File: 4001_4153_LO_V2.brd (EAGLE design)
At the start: 109 x 63 mm, 112 parts, among them IC1 74LVC2G17GV,125, IC10 MCP6H01, IC2 74LVC2G17GV,125, IC3 74LVC2G17GV,125, IC4 ADF4001BRUZ, IC5 ATTINY45V-10SU, IC6 7805DT, IC7 7809DT, IC8 LD1117AS33TR, IC9 ADF4153BRUZ-RL7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

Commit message: JLC release
As issued to JLC
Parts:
- added C4: 100nF, rcl:C0603
- added IC11: TL431AIDBZR, RF:SOT23L
- added R30: 470R, rcl:R0603
- added R31, R32: 10K, rcl:R0603
- IC10: value MCP6H01 -> MCP6H01T-E/LT
- moved C23 27.7 mm to (36.9, 5.57), turned to 270 degrees
- moved C20 12.6 mm to (13.9, 34.4), turned to 90 degrees
- moved C21 12.0 mm to (11.9, 34.4), turned to 90 degrees
- moved LSP1 11.0 mm to (17.9, 23.2)
- moved IC7 4.91 mm to (9.24, 29.0), turned to 90 degrees
- moved TXFMR1 4.02 mm to (11.2, 44.9)
- moved C19 2.84 mm to (11.5, 23.3), turned to 180 degrees
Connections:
- new net +5V_PRECISION: C4.1, IC11.G, R30.2, R32.2, VR1.3
- new net N$42: IC11.S, R31.2, R32.1
- net +12V: now also R30.1
- net +5V: no longer VR1.3
- net GND: now also C4.2, IC11.D, R31.1, TXFMR1.1, TXFMR1.6; no longer TXFMR1.3, TXFMR1.4
- net N$33: now also TXFMR1.4; no longer TXFMR1.6
- net N$34: now also TXFMR1.3; no longer TXFMR1.1
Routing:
- net +5V_PRECISION: track 0.00 -> 42.2 mm, vias 0 -> 1
- net +5V: track 158.1 -> 128.1 mm
- net +12V: track 52.0 -> 63.6 mm, vias 2 -> 4
- net N$42: track 0.00 -> 4.41 mm
- net GND: track 59.0 -> 54.9 mm, vias 188 -> 193
- net +9V: track 125.0 -> 128.1 mm

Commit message: various
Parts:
- removed R19: 51R, rcl:R0603
- C22: value 100nF -> 100pF; device rcl:C0805 -> resistor:C0603
- IC10: value MCP6H01T-E/LT -> TS971ILT
- R18: value 18K -> 22R
- moved C23 29.3 mm to (66.2, 5.72), turned to 0 degrees
- moved C29 18.5 mm to (65.6, 24.7), turned to 90 degrees
- moved C22 7.57 mm to (81.4, 21.8), turned to 90 degrees
- moved R21 5.57 mm to (85.6, 6.35)
- turned OSC1 to 180 degrees
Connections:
- removed net CLK: IC4.11, IC9.11
- new net +5V_VCO: L6.2
- net +9V: no longer C22.1, L6.2
- net GND: no longer R19.1
- net N$1: now also C22.1; no longer R19.2
- net SCK: now also IC4.11, IC9.11
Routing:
- net SCK: track 5.78 -> 60.8 mm, vias 0 -> 1
- net 20_MHZ: track 63.2 -> 26.8 mm
- net CLK: track 28.6 -> 0.00 mm
- net +9V: track 128.1 -> 109.7 mm, vias 3 -> 2
- net N$32: track 39.8 -> 27.3 mm
- net MOSI: track 9.37 -> 19.1 mm
- net MISO: track 17.4 -> 11.8 mm
- net 10MHZ_REF: track 14.4 -> 19.9 mm
- net GND: track 54.9 -> 51.2 mm, vias 193 -> 201
- net +3V3: track 276.7 -> 274.0 mm
- net N$8: track 6.09 -> 3.69 mm
- net +5V: track 128.1 -> 130.2 mm
- net LOOP_IN: track 11.6 -> 12.8 mm

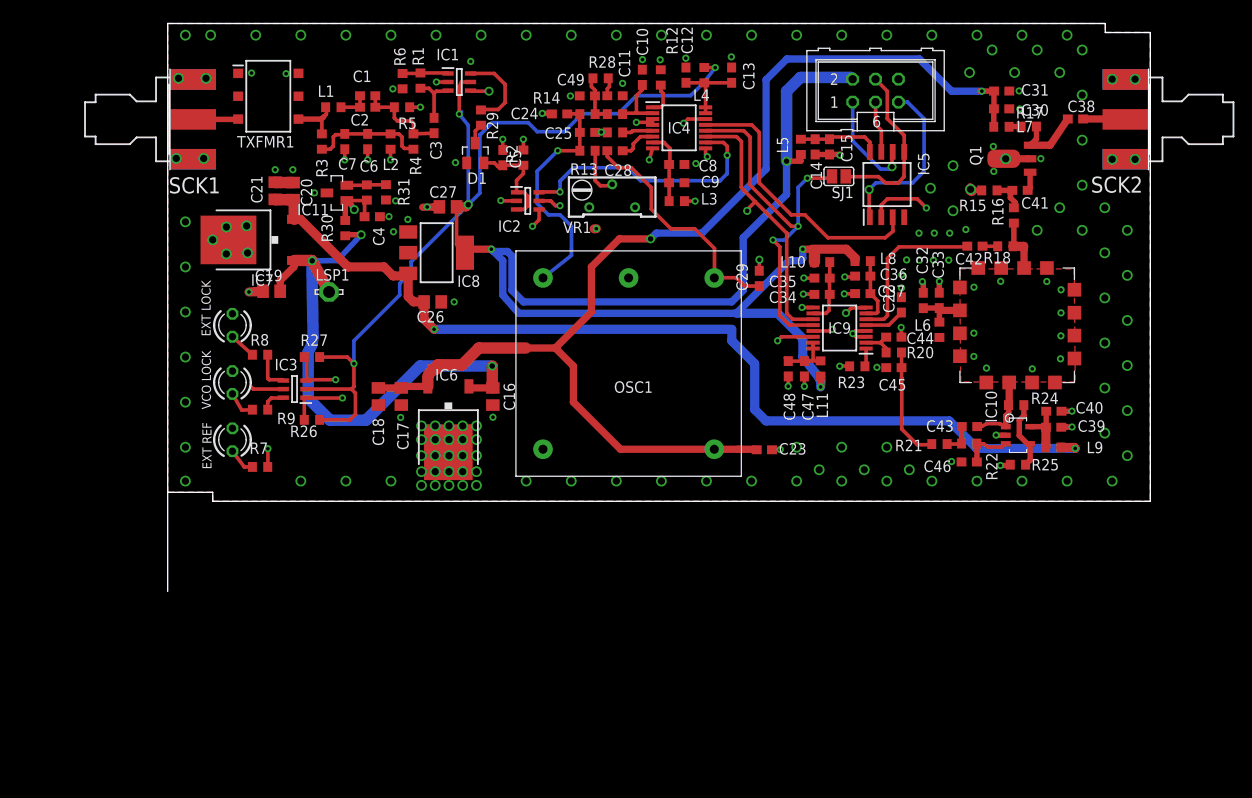
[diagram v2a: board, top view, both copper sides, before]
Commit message: filter loop update
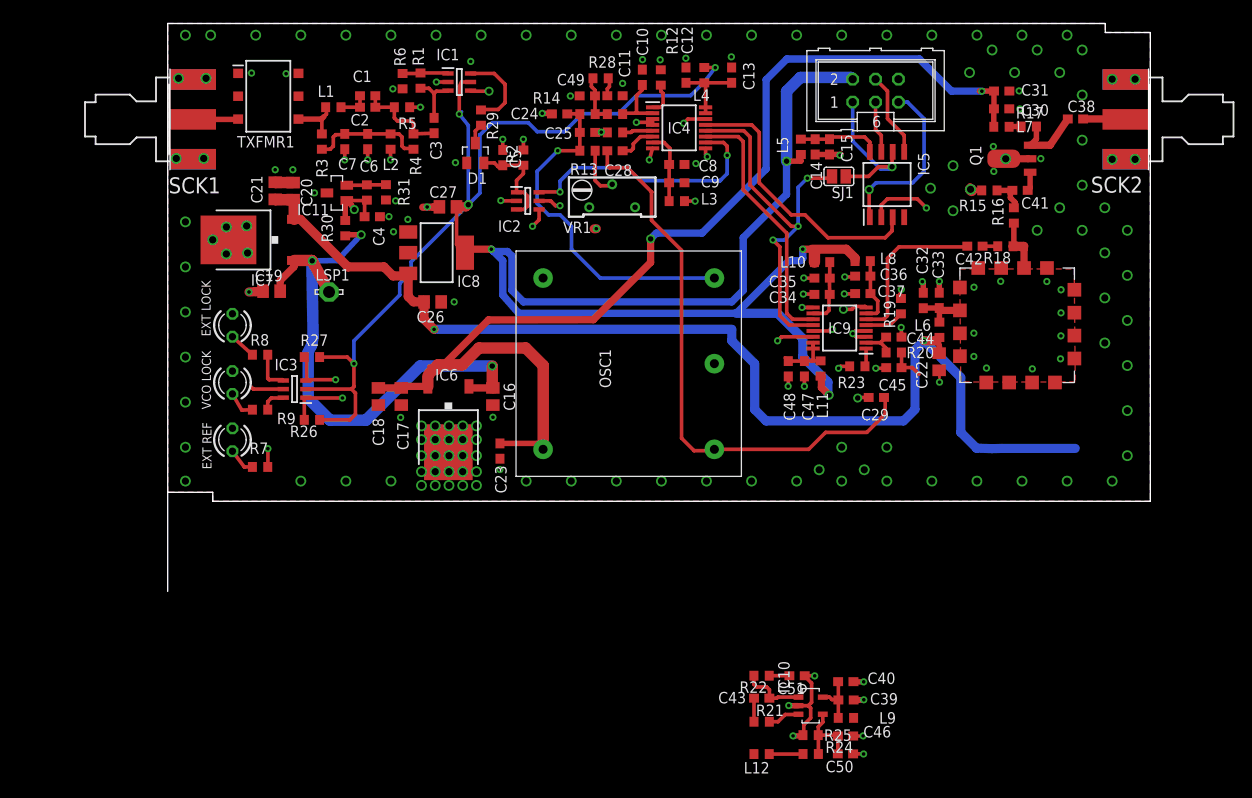
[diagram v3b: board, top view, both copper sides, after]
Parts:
- added C50: 100pF, resistor:C0603
- added C51: 100nF, resistor:C0603
- added L12: 100nH, resistor:R0603
- added R19: 51R, rcl:R0603
- C22: value 100pF -> 100nF; device resistor:C0603 -> rcl:C0805
- C43: value 6.8nF -> 27nF
- C44: value 22nF -> 10nF
- C45: value 10nF -> 1.2nF
- C46: value 15nF -> 100nF
- IC10: value TS971ILT -> MCP6H01T-E/LT
- R18: value 22R -> 18K
- R21: value 27k -> 560R
- R22: value 39k -> 560R
- R24: value 18K -> 10K
- moved R24 44.9 mm to (71.3, -28.0)
- moved C39 38.0 mm to (75.2, -22.0)
- moved C43 37.9 mm to (65.9, -21.8)
- moved C40 37.8 mm to (75.2, -20.0)
- moved IC10 37.8 mm to (71.3, -22.7)
- moved L9 37.8 mm to (75.2, -24.0)
- moved R25 37.8 mm to (71.3, -25.9)
- moved R21 36.6 mm to (65.9, -24.4)
- moved R22 34.5 mm to (65.9, -19.3), turned to 180 degrees
- moved C46 33.4 mm to (75.2, -26.0), turned to 180 degrees
- moved C23 29.3 mm to (36.9, 5.57), turned to 270 degrees
- moved C29 18.5 mm to (78.6, 11.5), turned to 180 degrees
- moved C22 7.57 mm to (85.6, 15.5), turned to 270 degrees
- turned OSC1 to 90 degrees
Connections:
- removed net +5V_VCO: L6.2
- removed net N$6: C43.2, IC10.P$1, OSC2.P$2, R24.2
- new net CLK: IC4.11, IC9.11
- new net N$39: L12.1, R24.2
- new net N$40: C51.2, OSC2.P$2, R22.1
- net +3V3: now also L12.2
- net +9V: now also C22.1, L6.2
- net GND: now also C50.1, C51.1, R19.1
- net LOOP_IN: now also IC10.P$3, R21.2; no longer R21.1
- net N$1: now also R19.2; no longer C22.1
- net N$5: now also C46.2, C50.2
- net N$8: now also R21.1; no longer R21.2, R22.1
- net N$9: now also C43.2, IC10.P$1; no longer C46.2, IC10.P$3
- net SCK: no longer IC4.11, IC9.11
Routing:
- net SCK: track 60.8 -> 5.78 mm, vias 1 -> 0
- net 20_MHZ: track 26.8 -> 63.2 mm
- net CLK: track 0.00 -> 28.6 mm
- net +9V: track 109.7 -> 126.5 mm
- net GND: track 51.2 -> 66.5 mm, vias 201 -> 191
- net N$32: track 27.3 -> 39.8 mm
- net MOSI: track 19.1 -> 9.37 mm
- net N$6: track 8.55 -> 0.00 mm
- net MISO: track 11.8 -> 17.4 mm
- net 10MHZ_REF: track 19.9 -> 14.4 mm
- net LOOP_IN: track 12.8 -> 7.67 mm
- net N$39: track 0.00 -> 3.75 mm
- net +3V3: track 274.0 -> 276.7 mm
- net N$40: track 0.00 -> 2.24 mm
- net +5V: track 130.2 -> 128.1 mm
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
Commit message: Layout
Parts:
- added C52: DNF, resistor:C0603
- moved L12 44.5 mm to (87.1, 11.0), turned to 0 degrees
- moved R24 40.4 mm to (81.7, 11.0), turned to 0 degrees
- moved C50 39.1 mm to (77.8, 11.0), turned to 0 degrees
- moved R21 37.8 mm to (87.1, 6.86), turned to 180 degrees
- moved R25 36.4 mm to (81.7, 8.94), turned to 0 degrees
- moved C46 35.2 mm to (77.8, 9.03), turned to 0 degrees
- moved R22 34.4 mm to (90.4, 4.80)
- moved C43 34.1 mm to (87.1, 4.84), turned to 180 degrees
- moved C51 33.4 mm to (90.4, 6.90), turned to 0 degrees
- moved IC10 30.2 mm to (81.7, 5.67), turned to 180 degrees
- moved L9 29.1 mm to (72.5, 4.99), turned to 180 degrees
- moved C39 27.2 mm to (77.8, 5.03), turned to 180 degrees
- moved C40 27.2 mm to (77.8, 7.04), turned to 180 degrees
- moved C29 9.27 mm to (69.4, 10.5), turned to 0 degrees
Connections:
- net LOOP_IN: now also C52.1
- net N$8: now also C52.2
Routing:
- net +3V3: track 276.7 -> 294.0 mm, vias 10 -> 11
- net 20_MHZ: track 63.2 -> 52.4 mm
- net GND: track 66.5 -> 55.8 mm, vias 191 -> 187
- net LOOP_IN: track 7.67 -> 16.4 mm, vias 0 -> 2
- net N$40: track 2.24 -> 9.68 mm
- net N$3: track 5.95 -> 10.9 mm
- net 10MHZ_REF: track 14.4 -> 16.5 mm
- net +9V: track 126.5 -> 124.3 mm, vias 2 -> 4
- net N$9: track 7.15 -> 8.73 mm
- net N$8: track 2.61 -> 4.04 mm

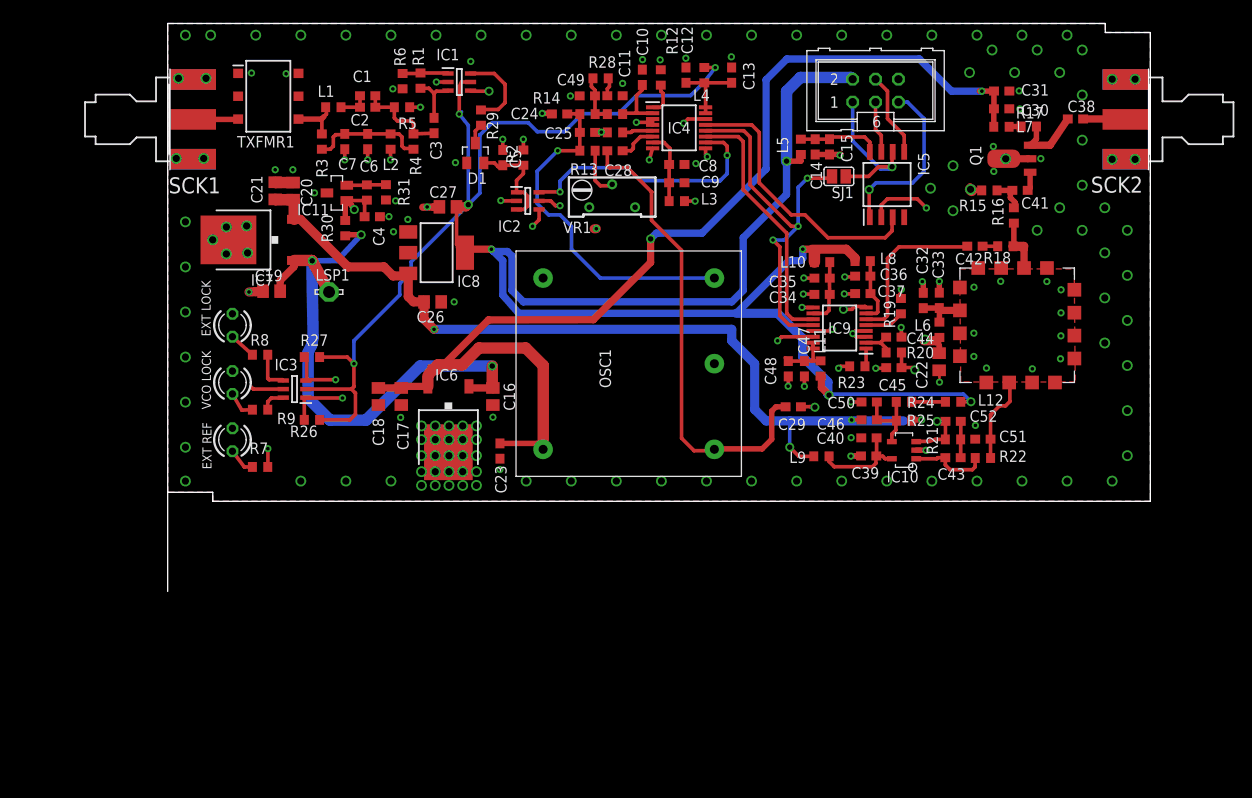
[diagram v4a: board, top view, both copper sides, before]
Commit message: Ref synth updates
Firmware working for ADF4001
Various board updates, ref input still needs works
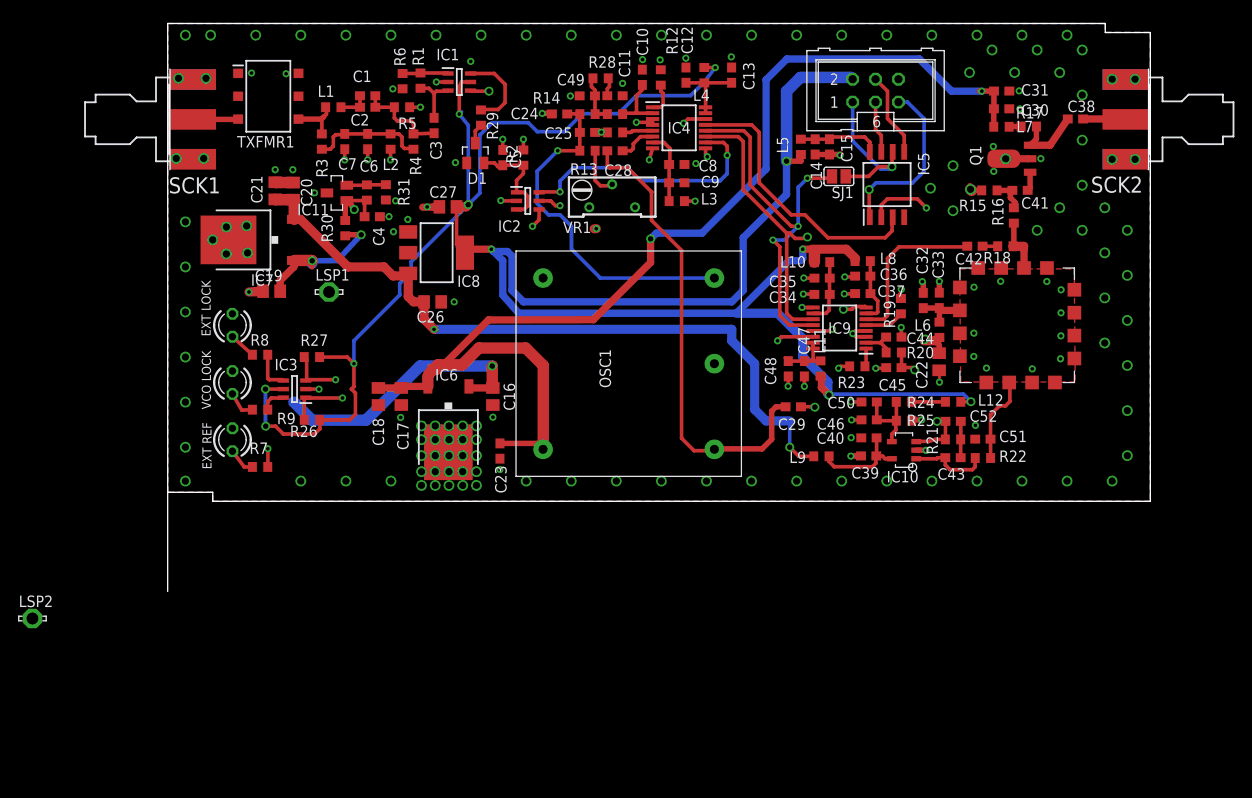
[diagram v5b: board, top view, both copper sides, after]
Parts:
- added LSP2: LSP13, solpad:LSP13
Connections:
- net 20_MHZ renamed 10MHZ
- net 20_MHZ_4001 renamed 10_MHZ_4001
- removed net CLK: IC4.11, IC9.11
- new net +12V_OSC: C16.1, IC6.1, LSP2.MP
- net +12V: no longer C16.1, IC6.1
- net +3V3: now also IC3.5; no longer IC3.2
- net GND: now also IC3.2; no longer IC3.5
- net SCK: now also IC4.11, IC9.11
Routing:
- net SCK: track 5.78 -> 55.7 mm, vias 0 -> 1
- net +12V: track 63.6 -> 15.5 mm, vias 4 -> 3
- net +12V_OSC: track 0.00 -> 30.5 mm, vias 0 -> 1
- net CLK: track 28.6 -> 0.00 mm
- net +9V: track 124.3 -> 111.7 mm
- net +3V3: track 294.0 -> 302.7 mm, vias 11 -> 13
- net GND: track 55.8 -> 53.6 mm, vias 187 -> 188
